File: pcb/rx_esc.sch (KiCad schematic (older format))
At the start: 54 parts, among them CON1 AVR-ISP-6, J1 CONN_01X02, J2 CONN_01X02, J3 CONN_02X06, J4 CONN_01X03, J5 CONN_01X03, J6 CONN_01X02, J7 CONN_01X02, Q1 Q_NMOS_DGS, Q2 Q_NMOS_DGS, Q3 Q_NMOS_DGS, Q4 Q_NMOS_DGS, Q5 Q_NMOS_DGS, Q6 Q_NMOS_DGS, U1 A3906, U2 ATMEGA328PB-AU, U3 NRF24L01_MODULE, Y1 Crystal

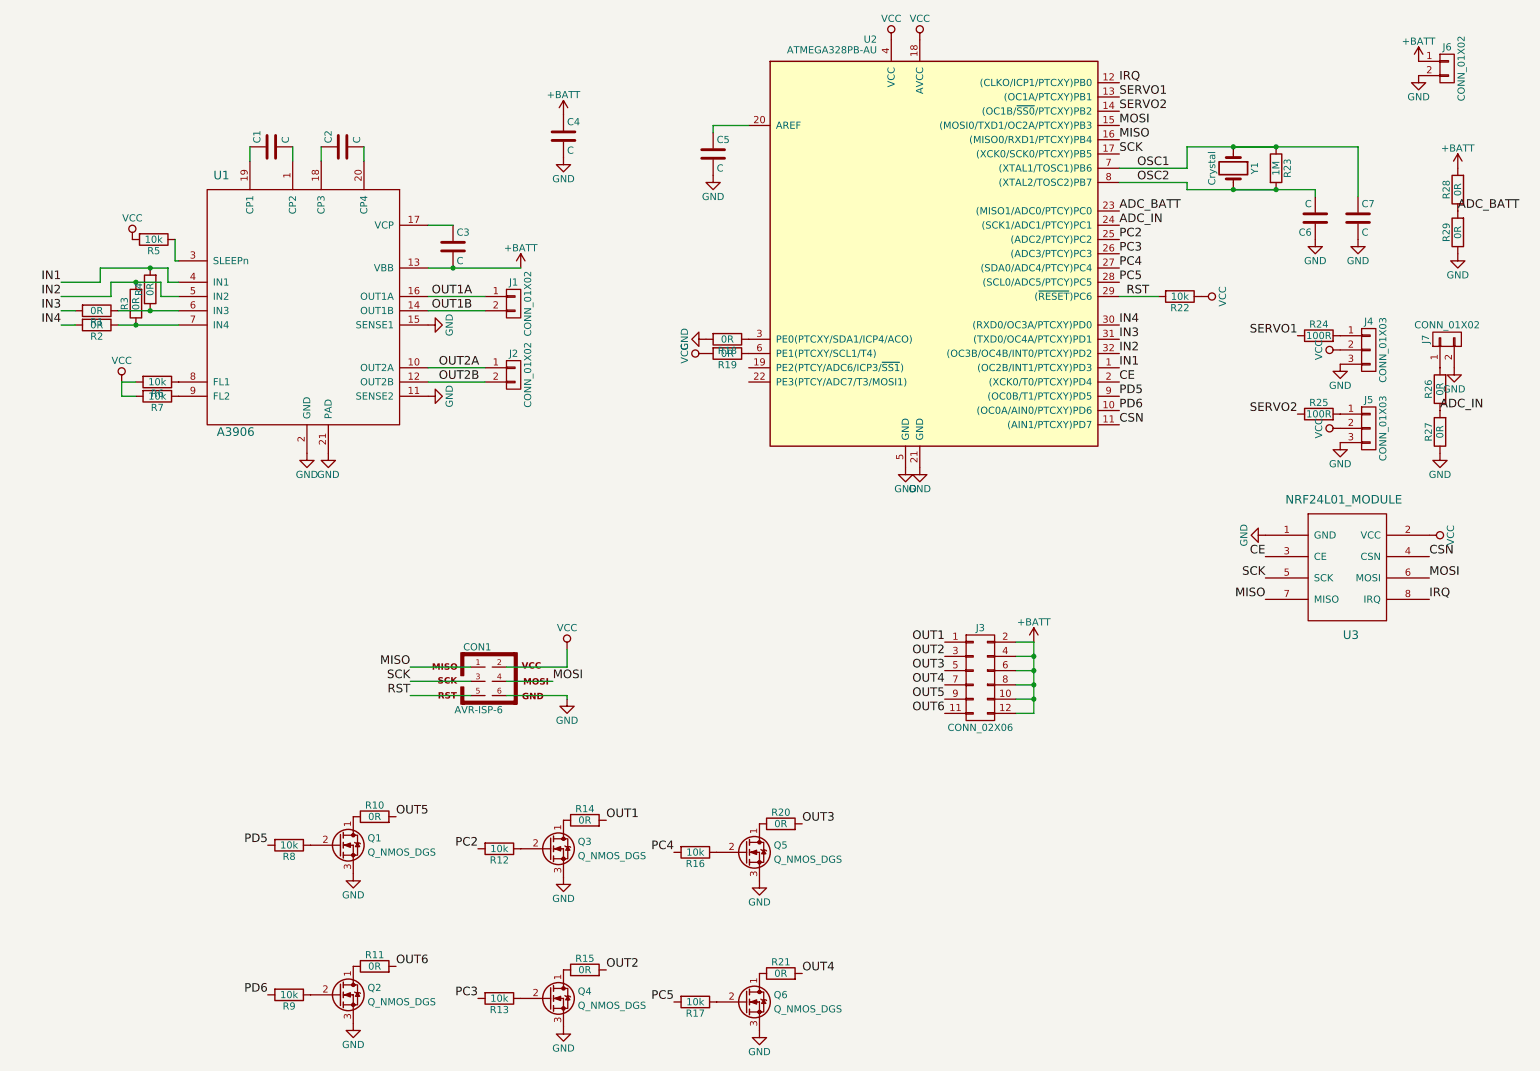
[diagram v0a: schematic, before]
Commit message: VE 24-12-17 Add power supply
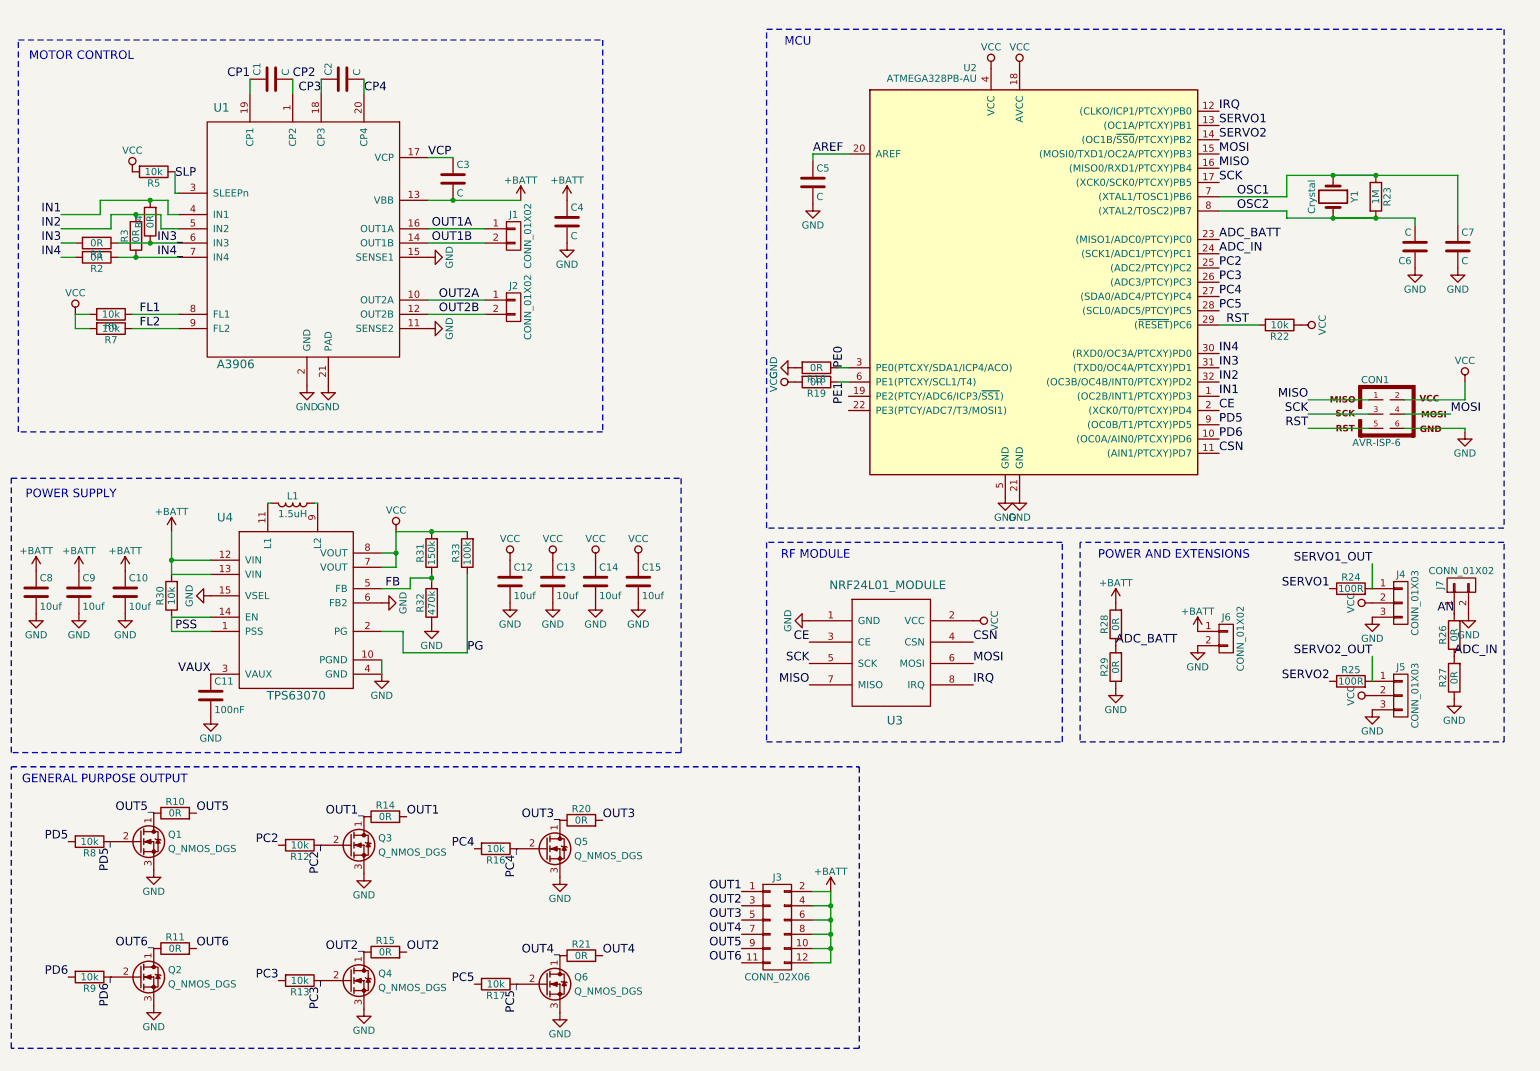
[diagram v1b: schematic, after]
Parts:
- added C10, C13, C14, C15, C9: 10uf, Capacitors_SMD:C_0805, symbol C
- added C11: 100nF, Capacitors_SMD:C_0402, symbol C
- added C12, C8: 10uf, Capacitors_SMD:C_0603, symbol C
- added L1: 1.5uH, Inductors_SMD:L_Coilcraft_XAL5030, symbol L
- added R30: 10k, Resistors_SMD:R_0402, symbol R
- added R31: 150k, Resistors_SMD:R_0402, symbol R
- added R32: 470k, Resistors_SMD:R_0402, symbol R
- added R33: 100k, Resistors_SMD:R_0402, symbol R
- added U4: TPS63070, FOOTPRINT:QFN-16-1EP_3x3mm_Pitch0.5mm, symbol TPS63070
- C4: footprint Capacitors_SMD:C_0402 -> Capacitors_SMD:C_0603
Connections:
- net +BATT: now also C10.1, C8.1, C9.1, R30.2, U4.12 (VIN), U4.13 (VIN)
- net GND: now also C10.2, C11.2, C12.2, C13.2, C14.2, C15.2, C8.2, C9.2, R32.1, U4.10 (PGND), U4.15 (VSEL), U4.4 (GND), U4.6 (FB2)
- net VCC: now also C12.1, C13.1, C14.1, C15.1, R31.2, R33.2, U4.7 (VOUT), U4.8 (VOUT)
- net AREF: now reaches C5.1, U2.20 (AREF)
- net OUT5_: now reaches Q1.1 (D), R10.1
- net PD5_: now reaches Q1.2 (G), R8.1
- net OUT6_: now reaches Q2.1 (D), R11.1
- net PD6_: now reaches Q2.2 (G), R9.1
- net OUT1_: now reaches Q3.1 (D), R14.1
- net PC2_: now reaches Q3.2 (G), R12.1
- net OUT2_: now reaches Q4.1 (D), R15.1
- net PC3_: now reaches Q4.2 (G), R13.1
- net OUT3_: now reaches Q5.1 (D), R20.1
- net PC4_: now reaches Q5.2 (G), R16.1
- net OUT4_: now reaches Q6.1 (D), R21.1
- net PC5_: now reaches Q6.2 (G), R17.1
- net CP2: now reaches C1.2, U1.1 (CP2)
- net VCP: now reaches C3.1, U1.17 (VCP)
- net CP3: now reaches C2.1, U1.18 (CP3)
- net CP1: now reaches C1.1, U1.19 (CP1)
- net CP4: now reaches C2.2, U1.20 (CP4)
- net SLP: now reaches R5.1, U1.3 (SLEEPn)
- net IN3_: now reaches R1.1, R4.1, U1.6 (IN3)
- net IN4_: now reaches R2.1, R3.1, U1.7 (IN4)
- net FL1: now reaches R6.1, U1.8 (FL1)
- net FL2: now reaches R7.1, U1.9 (FL2)
- net PE0: now reaches R18.1, U2.3 (PE0(PTCXY/SDA1/ICP4/ACO))
- net PE1: now reaches R19.1, U2.6 (PE1(PTCXY/SCL1/T4))
- net SERVO2_OUT: now reaches J5.1 (P1), R25.2
- net SERVO1_OUT: now reaches J4.1 (P1), R24.2
- net AN: now reaches J7.1 (P1), R26.2
- new net: L1.1, U4.9 (L2)
- new net: L1.2, U4.11 (L1)
- new net FB: R31.1, R32.2, U4.5 (FB)
- new net PG: R33.1, U4.2 (PG)
- new net PSS: R30.1, U4.1 (PSS), U4.14 (EN)
- new net VAUX: C11.1, U4.3 (VAUX)
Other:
- note added: "GENERAL PURPOSE OUTPUT"
- note added: "MCU"
- note added: "MOTOR CONTROL"
- note added: "POWER AND EXTENSIONS"
- note added: "POWER SUPPLY"
- note added: "RF MODULE"
- moved on the sheet: C1, C2, C3, C4, C5, C6, C7, CON1, J1, J2, J3, J4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

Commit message: VE 25-12-17 PCB routed schematic updated
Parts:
- C1, C2: footprint Capacitors_SMD:C_0402 -> Capacitors_SMD:C_0603
- Q1, Q2, Q3, Q4, Q5, Q6: value Q_NMOS_DGS -> MMBT2222; symbol Q_NMOS_DGS -> Q_NPN_BEC
- R1, R2, R3, R4: footprint Resistors_SMD:R_0402 -> Resistors_SMD:R_0603
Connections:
- net ADC_BATT: now also U2.24 ((SCK1/ADC1/PTCY)PC1); no longer U2.23 ((MISO1/ADC0/PTCY)PC0)
- net ADC_IN: now also U2.23 ((MISO1/ADC0/PTCY)PC0); no longer U2.24 ((SCK1/ADC1/PTCY)PC1)
- net CE: now also U2.9 ((OC0B/T1/PTCXY)PD5); no longer U2.2 ((XCK0/T0/PTCXY)PD4)
- net GND: now also Q1.2 (E), Q2.2 (E), Q3.2 (E), Q4.2 (E), Q5.2 (E), Q6.2 (E); no longer Q1.3 (S), Q2.3 (S), Q3.3 (S), Q4.3 (S), Q5.3 (S), Q6.3 (S)
- net OUT1_: now also Q3.3 (C); no longer Q3.1 (D)
- net OUT2_: now also Q4.3 (C); no longer Q4.1 (D)
- net OUT3_: now also Q5.3 (C); no longer Q5.1 (D)
- net OUT4_: now also Q6.3 (C); no longer Q6.1 (D)
- net OUT5_: now also Q1.3 (C); no longer Q1.1 (D)
- net OUT6_: now also Q2.3 (C); no longer Q2.1 (D)
- net PC2: now also R17.2; no longer R12.2
- net PC2_: now also Q6.1 (B), R17.1; no longer Q3.2 (G), R12.1
- net PC3: now also R16.2; no longer R13.2
- net PC3_: now also Q5.1 (B), R16.1; no longer Q4.2 (G), R13.1
- net PC4: now also R13.2; no longer R16.2
- net PC4_: now also Q4.1 (B), R13.1; no longer Q5.2 (G), R16.1
- net PC5: now also R12.2; no longer R17.2
- net PC5_: now also Q3.1 (B), R12.1; no longer Q6.2 (G), R17.1
- net PD6_: now also Q2.1 (B); no longer Q2.2 (G)
- net PD5 renamed PD4
- net PD4: now also U2.2 ((XCK0/T0/PTCXY)PD4); no longer U2.9 ((OC0B/T1/PTCXY)PD5)
- net PD5_ renamed PD4_
- net PD4_: now also Q1.1 (B); no longer Q1.2 (G)
